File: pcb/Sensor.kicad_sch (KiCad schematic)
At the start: 34 parts, among them IC2 74HC14D-Q100,118, U2 OPA2376AIDR, U4 OPA2376AIDR

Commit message: added digital input for QS
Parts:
- added C27: 100n, Capacitor_SMD:C_0201_0603Metric, symbol Device:C
- added D16: D, symbol Device:D
- added R53: 10k, Resistor_SMD:R_0201_0603Metric, symbol Device:R
- added R54: 1k, Resistor_SMD:R_0201_0603Metric, symbol Device:R
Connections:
- net +3V3: now also R53.2
- net GND: now also C27.1
- net DIGITAL_QS_IN: now reaches IC2.3 (2A)
- net DIGITAL_QS_IN: now also C27.2, D16.1 (K), R54.1
- net DIGITAL_QS_OUT: now reaches IC2.4 (2Y)
- new net: D16.2 (A), R53.1, R54.2
- no-connect marks 8 -> 9
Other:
- moved on the sheet: IC2, R22, R45, TP14, TP18

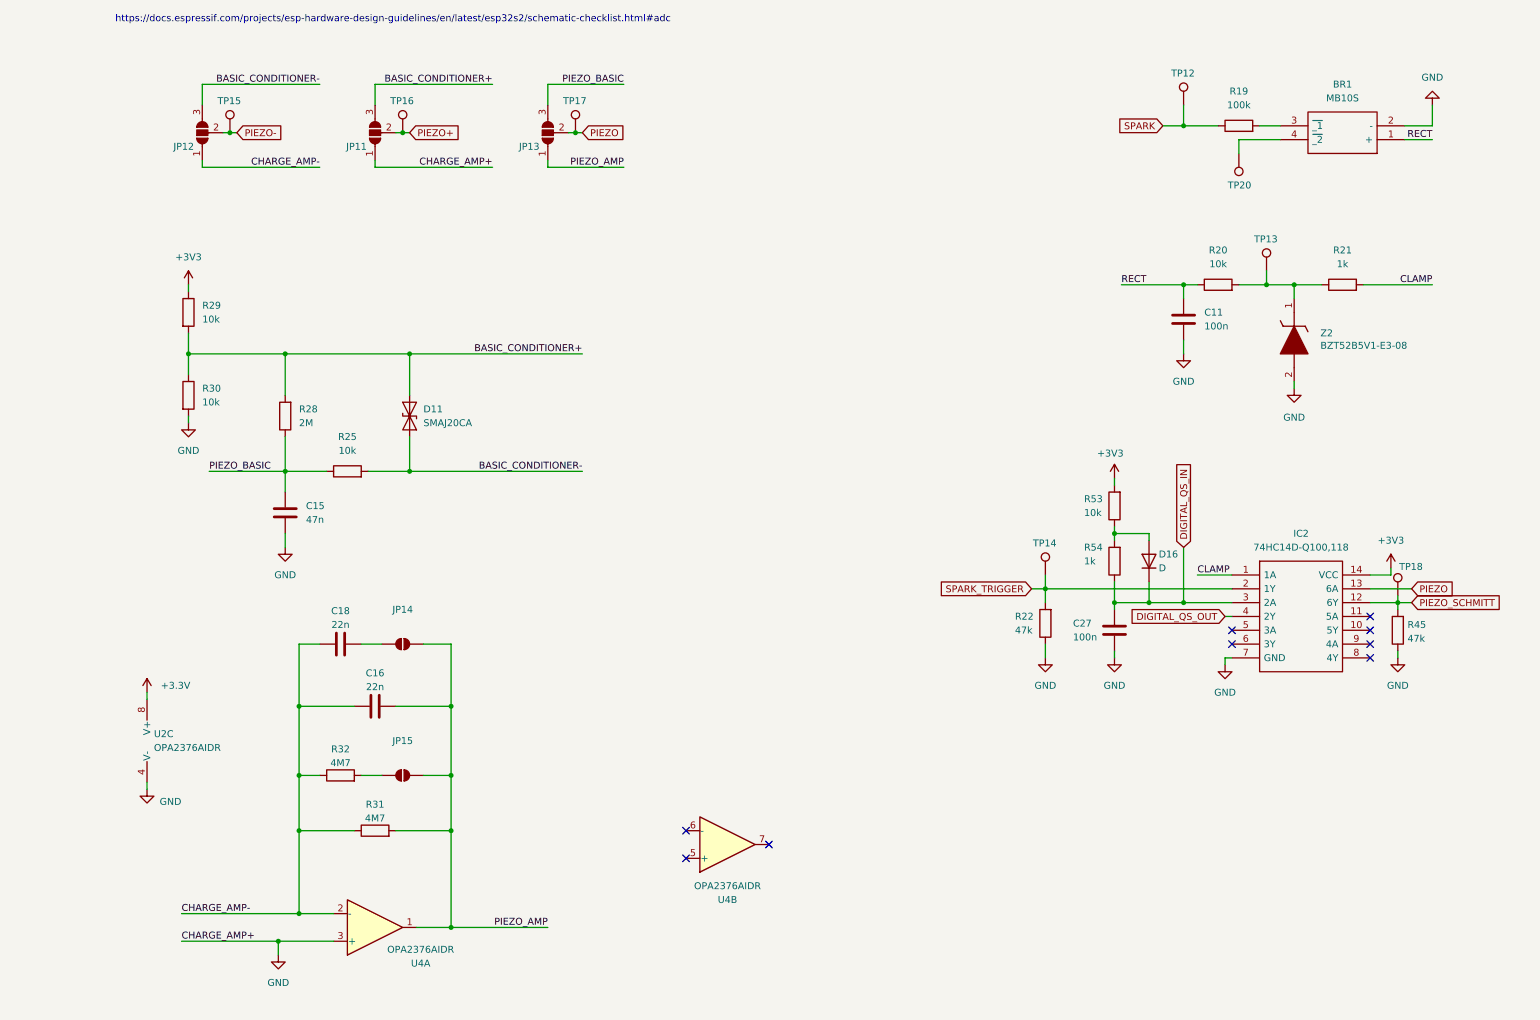
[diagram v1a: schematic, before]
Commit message: fixed basic pcb errors
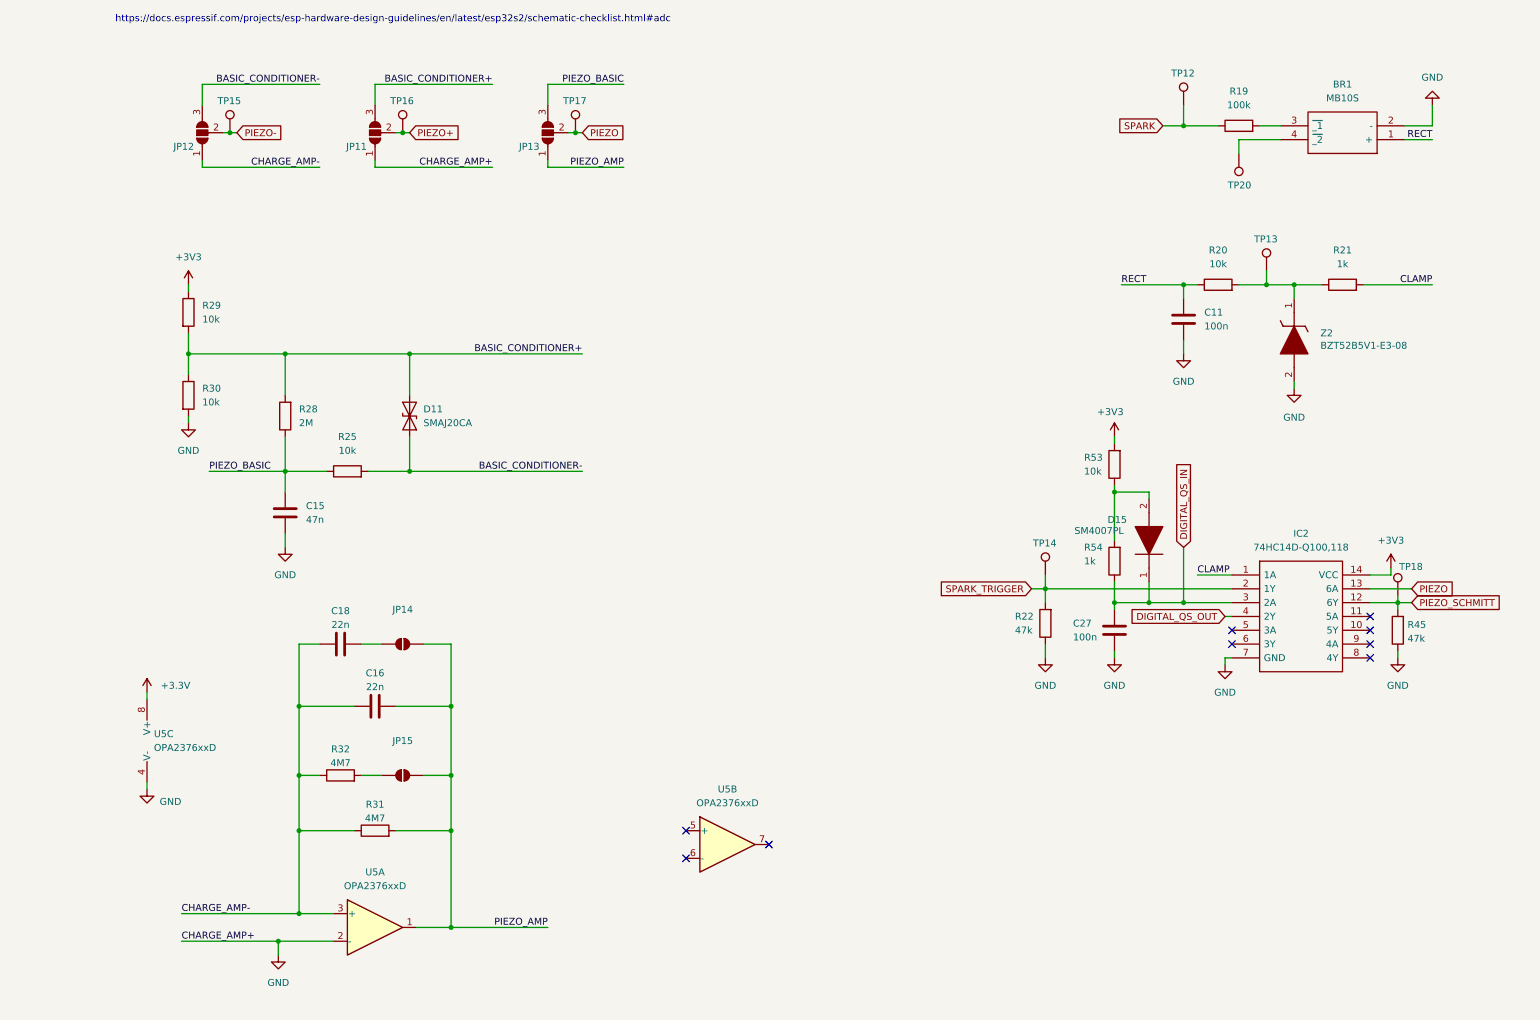
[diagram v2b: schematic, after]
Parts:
- removed D16: D, symbol Device:D
- removed U2, U4: OPA2376AIDR, symbol Amplifier_Operational:OPA2376xxD
- added D15: SM4007PL, SODFL3718X125N, symbol SamacSys_Parts:SM4007PL
- added U5: OPA2376xxD, SamacSys_Parts:SOIC127P600X175-8N, symbol Amplifier_Operational:OPA2376xxD
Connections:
- net +3.3V: now also U5.8 (V+)
- net CHARGE_AMP-: now also U5.3 (+)
- net DIGITAL_QS_IN: now also D15.1
- net GND: now also U5.2 (-), U5.4 (V-)
- net PIEZO_AMP: now also U5.1
- net at R53.1, R54.2: now also D15.2
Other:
- moved on the sheet: R53

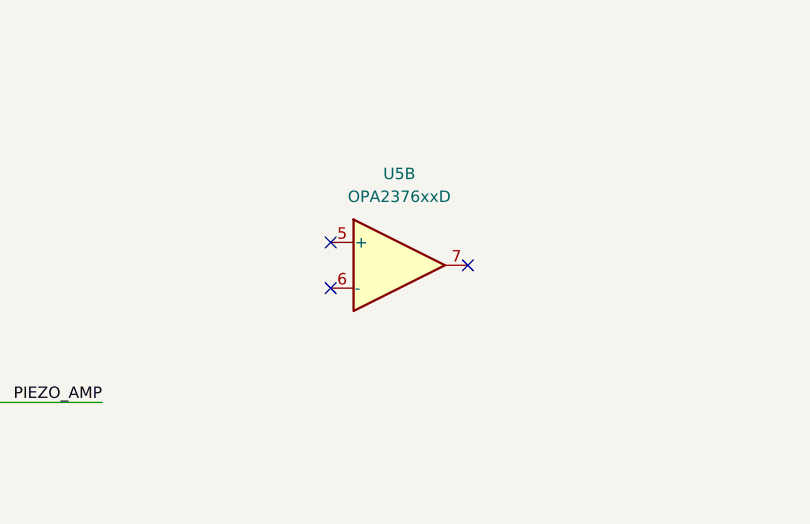
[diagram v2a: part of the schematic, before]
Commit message: enhanced pickup simulation
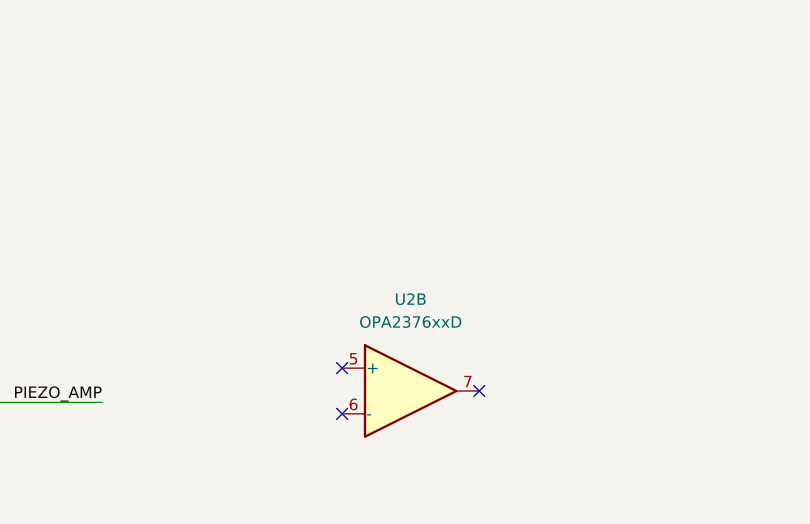
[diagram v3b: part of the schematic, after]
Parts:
- removed unit 2 of U5
- added U2: OPA2376xxD, SamacSys_Parts:SOIC127P600X175-8N, symbol Amplifier_Operational:OPA2376xxD
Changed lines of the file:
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@@
 	)
 	(no_connect
-		(at 140.97 165.1)
-	)
-	(no_connect
 		(at 226.06 125.73)
 	)
 	(no_connect
-		(at 125.73 167.64)
+		(at 142.24 179.07)
 	)
 	(no_connect
-		(at 125.73 162.56)
+		(at 251.46 128.27)
 	)
 	(no_connect
-		(at 251.46 128.27)
+		(at 127 176.53)
 	)
 	(no_connect
@@
 		(at 226.06 128.27)
 	)
+	(no_connect
+		(at 127 181.61)
+	)
 	(wire
 		(pts
@@
 	)
 	(symbol
-		(lib_id "Amplifier_Operational:OPA2376xxD")
-		(at 133.35 165.1 0)
-		(unit 2)
-		(exclude_from_sim no)
-		(in_bom yes)
-		(on_board yes)
-		(dnp no)
-		(fields_autoplaced yes)
-		(property "Reference" "U5"
-			(at 133.35 154.94 0)
-			(effects
-				(font
-					(size 1.27 1.27)
-				)
-			)
-		)
-		(property "Value" "OPA2376xxD"
-			(at 133.35 157.48 0)
-			(effects
-				(font
-					(size 1.27 1.27)
-				)
-			)
-		)
-		(property "Footprint" "SamacSys_Parts:SOIC127P600X175-8N"
-			(at 133.35 165.1 0)
-			(effects
-				(font
-					(size 1.27 1.27)
-				)
-				(hide yes)
-			)
-		)
-		(property "Datasheet" "http://www.ti.com/lit/ds/symlink/opa376.pdf"
-			(at 133.35 165.1 0)
-			(effects
-				(font
-					(size 1.27 1.27)
-				)
-				(hide yes)
-			)
-		)
-		(property "Description" "Dual Low-Noise, Low Quiescent Current, Precision Operational Amplifier e-trim Series, SOIC-8"
-			(at 133.35 165.1 0)
-			(effects
-				(font
-					(size 1.27 1.27)
-				)
-				(hide yes)
-			)
-		)
-		(pin "2"
-		)
-		(pin "1"
-		)
-		(pin "6"
-		)
-		(pin "3"
-		)
-		(pin "5"
-		)
-		(pin "8"
-		)
-		(pin "4"
-		)
-		(pin "7"
-		)
-		(instances
-			(project ""
-				(path "/38d4df77-b5a0-4642-8410-8b13c21c2c3b/4580a192-f0d7-44eb-b345-2965a93c3023"
-					(reference "U5")
-					(unit 2)
-				)
-			)
-		)
-	)
-	(symbol
 		(lib_id "power:+3.3V")
 		(at 26.67 137.16 0)
@@
 				)
 			)
+		)
+	)
+	(symbol
+		(lib_id "Amplifier_Operational:OPA2376xxD")
+		(at 134.62 179.07 0)
+		(unit 2)
+		(exclude_from_sim no)
+		(in_bom yes)
+		(on_board yes)
+		(dnp no)
+		(fields_autoplaced yes)
+		(property "Reference" "U2"
+			(at 134.62 168.91 0)
+			(effects
+				(font
+					(size 1.27 1.27)
+				)
+			)
+		)
+		(property "Value" "OPA2376xxD"
+			(at 134.62 171.45 0)
+			(effects
+				(font
+					(size 1.27 1.27)
+				)
+			)
+		)
+		(property "Footprint" "SamacSys_Parts:SOIC127P600X175-8N"
+			(at 134.62 179.07 0)
+			(effects
+				(font
+					(size 1.27 1.27)
+				)
+				(hide yes)
+			)
+		)
+		(property "Datasheet" "http://www.ti.com/lit/ds/symlink/opa376.pdf"
+			(at 134.62 179.07 0)
+			(effects
+				(font
+					(size 1.27 1.27)
+				)
+				(hide yes)
+			)
+		)
+		(property "Description" "Dual Low-Noise, Low Quiescent Current, Precision Operational Amplifier e-trim Series, SOIC-8"
+			(at 134.62 179.07 0)
+			(effects
+				(font
+					(size 1.27 1.27)
+				)
+				(hide yes)
+			)
+		)
+		(pin "2"
+		)
+		(pin "1"
+		)
+		(pin "6"
+		)
+		(pin "3"
+		)
+		(pin "5"
+		)
+		(pin "8"
+		)
+		(pin "4"
+		)
+		(pin "7"
+		)
+		(instances
+			(project "ecu-dev-board"
+				(path "/38d4df77-b5a0-4642-8410-8b13c21c2c3b/4580a192-f0d7-44eb-b345-2965a93c3023"
+					(reference "U2")
+					(unit 2)
+				)
+			)

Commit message: changed capacitors and resistors footprints from 0201 to 0603
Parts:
- C27: footprint Capacitor_SMD:C_0201_0603Metric -> Capacitor_SMD:C_0603_1608Metric
- D15: footprint SODFL3718X125N -> SamacSys_Parts:SODFL3718X125N
- R21, R22, R29, R30, R45, R53, R54: footprint Resistor_SMD:R_0201_0603Metric -> Resistor_SMD:R_0603_1608Metric
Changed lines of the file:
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@@
 			)
 		)
-		(property "Footprint" "Resistor_SMD:R_0201_0603Metric"
+		(property "Footprint" "Resistor_SMD:R_0603_1608Metric"
 			(at 246.38 64.008 90)
 			(effects
@@
 			)
 		)
-		(property "Footprint" "SODFL3718X125N"
+		(property "Footprint" "SamacSys_Parts:SODFL3718X125N"
 			(at 210.82 105.41 0)
 			(effects
@@
 			)
 		)
-		(property "Footprint" "Resistor_SMD:R_0201_0603Metric"
+		(property "Footprint" "Resistor_SMD:R_0603_1608Metric"
 			(at 258.318 125.73 90)
 			(effects
@@
 			)
 		)
-		(property "Footprint" "Capacitor_SMD:C_0201_0603Metric"
+		(property "Footprint" "Capacitor_SMD:C_0603_1608Metric"
 			(at 203.5048 121.92 0)
 			(effects
@@
 			)
 		)
-		(property "Footprint" "Resistor_SMD:R_0201_0603Metric"
+		(property "Footprint" "Resistor_SMD:R_0603_1608Metric"
 			(at 206.248 95.25 90)
 			(effects
@@
 			)
 		)
-		(property "Footprint" "Resistor_SMD:R_0201_0603Metric"
+		(property "Footprint" "Resistor_SMD:R_0603_1608Metric"
 			(at 32.512 82.55 90)
 			(effects
@@
 			)
 		)
-		(property "Footprint" "Resistor_SMD:R_0201_0603Metric"
+		(property "Footprint" "Resistor_SMD:R_0603_1608Metric"
 			(at 32.512 67.31 90)
 			(effects
@@
 			)
 		)
-		(property "Footprint" "Resistor_SMD:R_0201_0603Metric"
+		(property "Footprint" "Resistor_SMD:R_0603_1608Metric"
 			(at 206.248 113.03 90)
 			(effects
@@
 			)
 		)
-		(property "Footprint" "Resistor_SMD:R_0201_0603Metric"
+		(property "Footprint" "Resistor_SMD:R_0603_1608Metric"
 			(at 193.548 124.46 90)
 			(effects

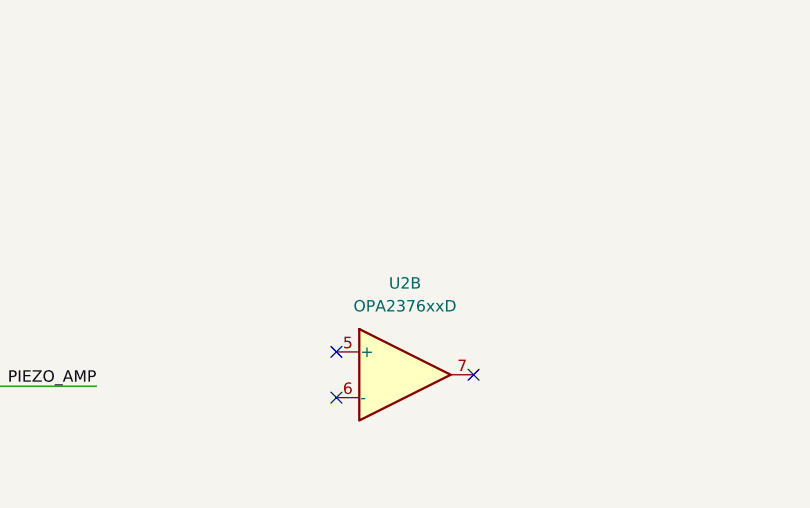
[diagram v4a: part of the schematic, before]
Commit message: changed SCR drives to pnp drive and started schematic revision
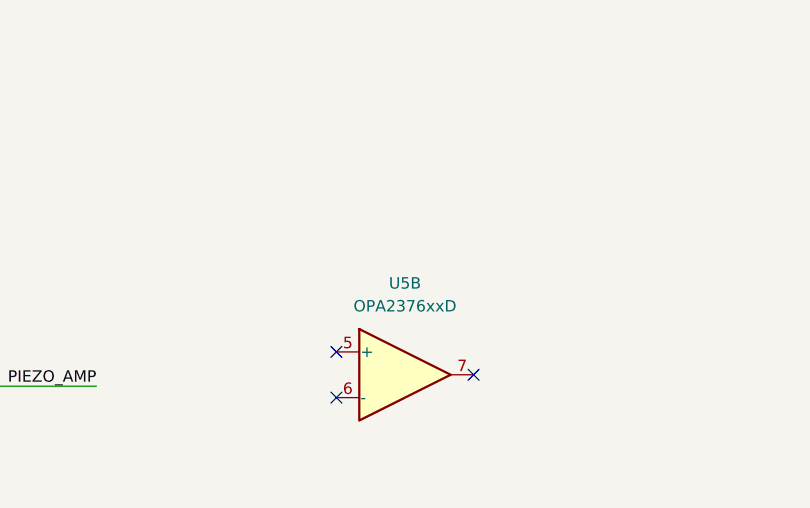
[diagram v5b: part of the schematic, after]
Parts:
- renumbered U2 to U5
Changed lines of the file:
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@@
 		(dnp no)
 		(fields_autoplaced yes)
-		(property "Reference" "U2"
+		(property "Reference" "U5"
 			(at 134.62 168.91 0)
 			(effects
@@
 			(project "ecu-dev-board"
 				(path "/38d4df77-b5a0-4642-8410-8b13c21c2c3b/4580a192-f0d7-44eb-b345-2965a93c3023"
-					(reference "U2")
+					(reference "U5")
 					(unit 2)
 				)

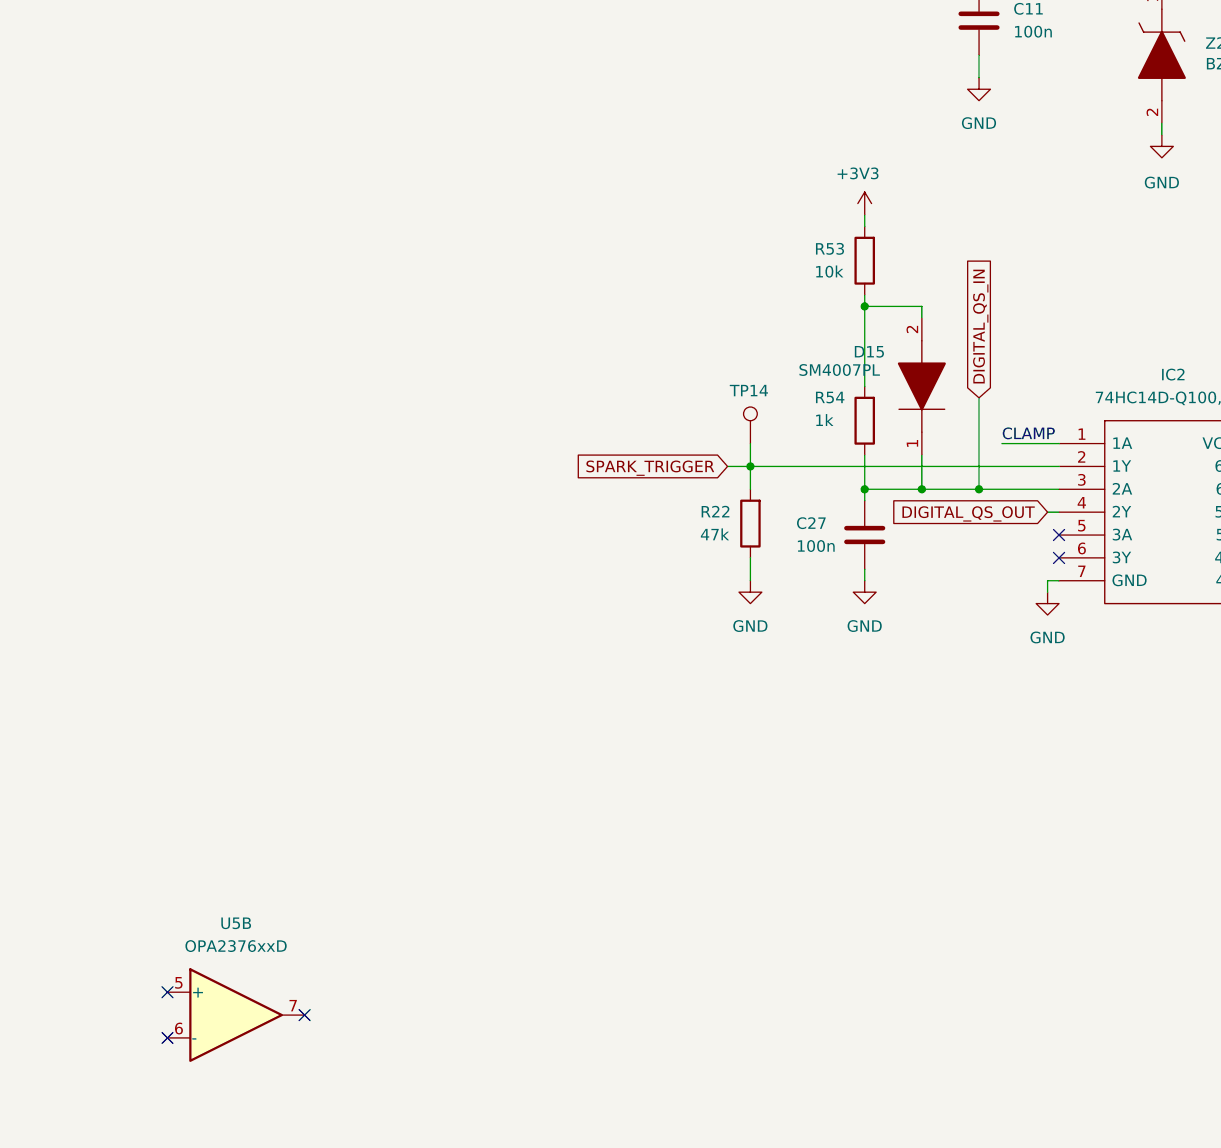
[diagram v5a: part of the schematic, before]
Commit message: added proper handling and comments to QS digital sensor
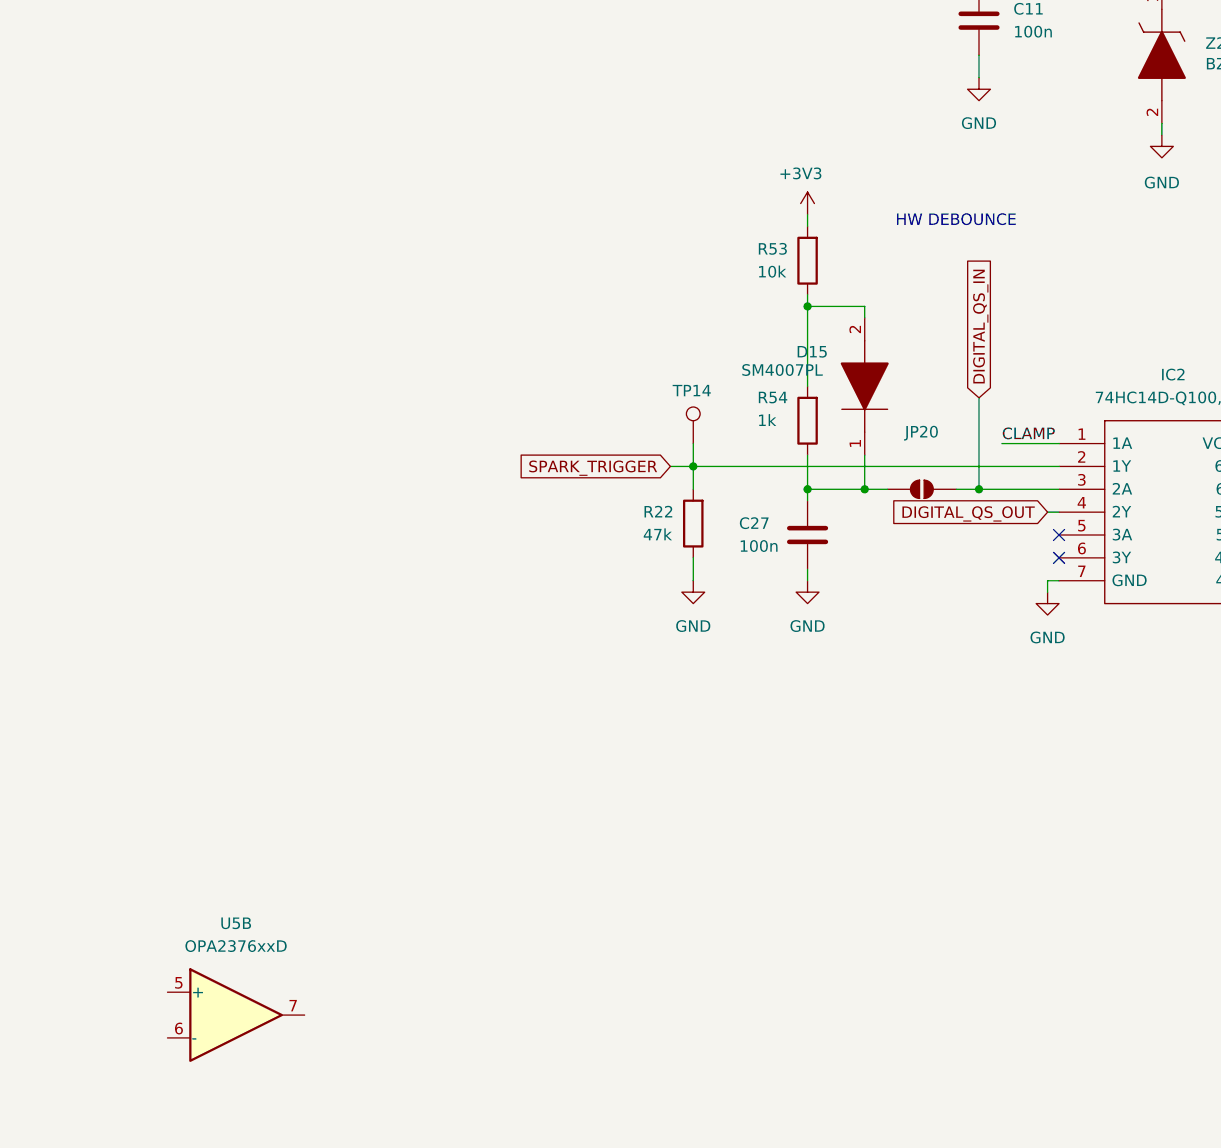
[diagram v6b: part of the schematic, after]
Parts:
- added JP20: SolderJumper_2_Open, Jumper:SolderJumper-2_P1.3mm_Open_RoundedPad1.0x1.5mm, symbol Jumper:SolderJumper_2_Open
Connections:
- net DIGITAL_QS_IN: now also JP20.1 (A); no longer C27.2, D15.1, R54.1
- new net: C27.2, D15.1, JP20.2 (B), R54.1
- no-connect marks 9 -> 6
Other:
- note added: "HW DEBOUNCE"
- moved on the sheet: C27, D15, R22, R53, R54, TP14
